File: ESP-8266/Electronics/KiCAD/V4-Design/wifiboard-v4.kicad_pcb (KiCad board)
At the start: 2 copper layers, 59 x 47 mm, 37 parts, among them IC1 78033AF, J1 PWR, J10 Conn_01x01_Male, J2 thermistor, J3 Aux1, J4 Aux2, J5 USB-3V3, J6 PROG, J7 OUT, J8 mains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

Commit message: SB & AB PCB layout
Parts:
- removed IC1: 78033AF, Package_TO_SOT_SMD:TO-252-2
- removed J10: Conn_01x01_Male, Connector_PinHeader_2.54mm:PinHeader_1x01_P2.54mm_Vertical
- added U2: 78033, Package_TO_SOT_SMD:TO-252-2, F.Cu at (50.9, 173.4)
- J9: value Conn_01x01_Male -> led-select; footprint Connector_PinHeader_2.54mm:PinHeader_1x01_P2.54mm_Vertical -> Connector_PinHeader_2.54mm:PinHeader_1x02_P2.54mm_Vertical
- moved R2 14.7 mm to (73.9, 158.6)
- moved R3 5.80 mm to (71.1, 144.3), turned to 270 degrees
- moved J9 2.67 mm to (48.0, 161.7), turned to 180 degrees
- moved C4 1.69 mm to (70.6, 140.0), turned to 90 degrees
- moved C1 1.63 mm to (39.2, 170.9)
- moved J1 1.27 mm to (30.1, 173.7)
- moved C3 1.19 mm to (63.0, 170.8)
- moved U1 0.09 mm to (67.1, 155.1)
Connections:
- R10 pad 1: Net-(J10-Pad1) -> Net-(J9-Pad1)
- R9 pad 2: Net-(J9-Pad1) -> Net-(J9-Pad2)
- U1 pad 14: Net-(J9-Pad1) -> Net-(J9-Pad2)
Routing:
- net +3V3: track 0.00 -> 129.2 mm, vias 0 -> 1
- net +12V: track 0.00 -> 68.6 mm
- net Net-(J5-Pad5): track 0.00 -> 38.6 mm
- net GND: track 0.00 -> 33.5 mm, vias 0 -> 2
- net Net-(J5-Pad4): track 0.00 -> 27.5 mm
- net Net-(J7-Pad2): track 0.00 -> 27.2 mm
- net Net-(C5-Pad1): track 0.00 -> 25.4 mm
- net Net-(C1-Pad1): track 0.00 -> 21.3 mm
- net Net-(J9-Pad2): track 0.00 -> 20.5 mm, vias 0 -> 1
- net Net-(C2-Pad1): track 0.00 -> 18.2 mm
- net Net-(J8-Pad2): track 0.00 -> 16.3 mm
- net Net-(J8-Pad1): track 0.00 -> 16.3 mm
- net Net-(J6-Pad2): track 0.00 -> 16.0 mm, vias 0 -> 2
- net Net-(R5-Pad2): track 0.00 -> 10.5 mm
- net Net-(J3-Pad1): track 0.00 -> 10.2 mm
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- added copper zone on B.Cu, net GND
- added copper zone on F.Cu, net GND
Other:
- board text added: "+12"
- board text added: "BLK"
- board text added: "GND"
- board text added: "GRN"
- board text added: "LED"
- board text added: "MAINS"
- board text added: "OUT"
- board text added: "PROG"
- board text added: "RESET"
- board text added: "Therm"
- board text added: "USB 3V3"

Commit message: PCB sent for trial production.
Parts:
- added JP1: SolderJumper_2_Bridged, Jumper:SolderJumper-2_P1.3mm_Bridged_RoundedPad1.0x1.5mm, F.Cu at (44.6, 160.4)
- moved R10 5.28 mm to (40.0, 163.4)
- moved J1 3.29 mm to (31.6, 176.7), turned to 270 degrees
- moved Q1 2.11 mm to (39.4, 144.4)
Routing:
- net Net-(J9-Pad2): track 20.5 -> 26.7 mm
- net Net-(J5-Pad5): track 38.6 -> 32.7 mm
- net Net-(J9-Pad1): track 3.76 -> 8.45 mm
- net Net-(J6-Pad2): track 16.0 -> 12.7 mm
- net Net-(Q1-Pad1): track 9.78 -> 12.1 mm
- net +3V3: track 129.2 -> 131.3 mm
- net Net-(J7-Pad2): track 27.2 -> 25.1 mm
- net Net-(D2-Pad2): track 2.52 -> 4.28 mm
- net +12V: track 68.6 -> 70.0 mm
- net Net-(C2-Pad1): track 18.2 -> 18.9 mm
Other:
- board text added: "L1"
- board text added: "L2"
- board text added: "POWER"

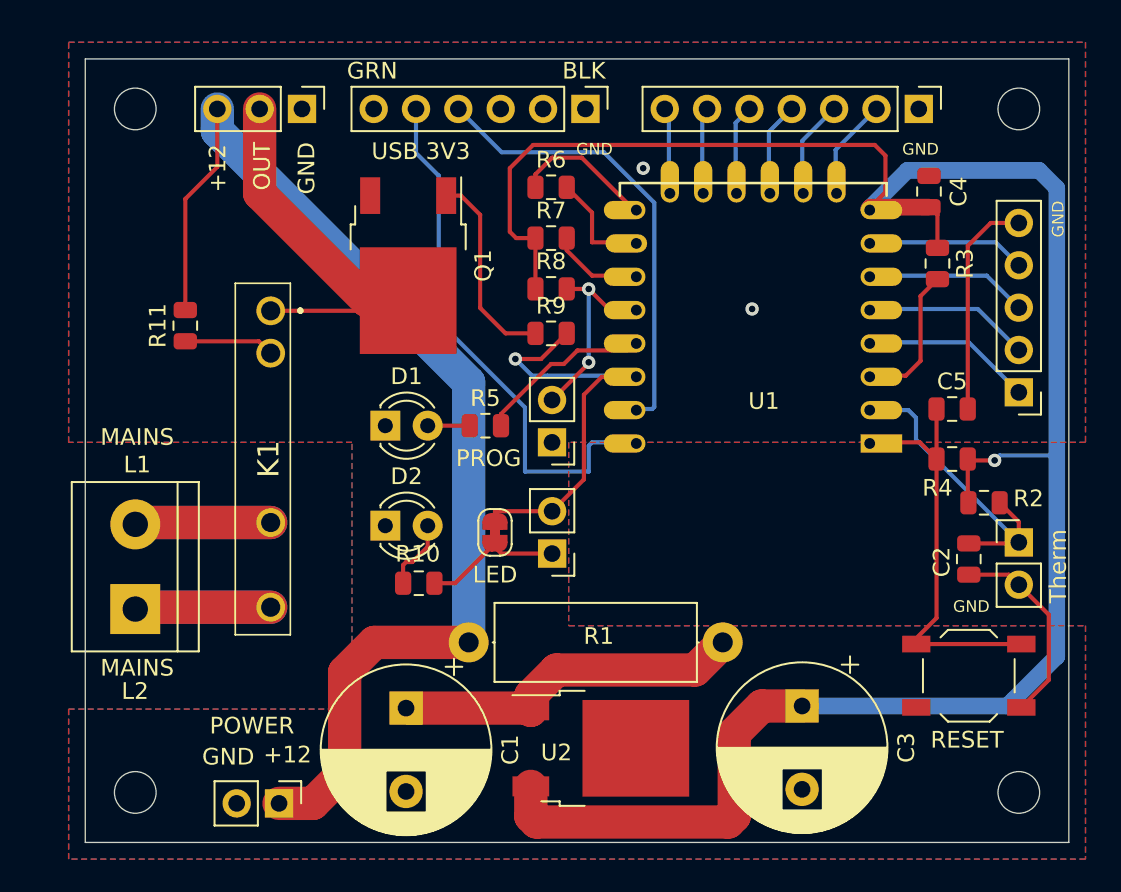
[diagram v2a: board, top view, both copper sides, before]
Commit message: PCB modified to accommodate relay as well as opto-SCR. GERBERS need to be updated.
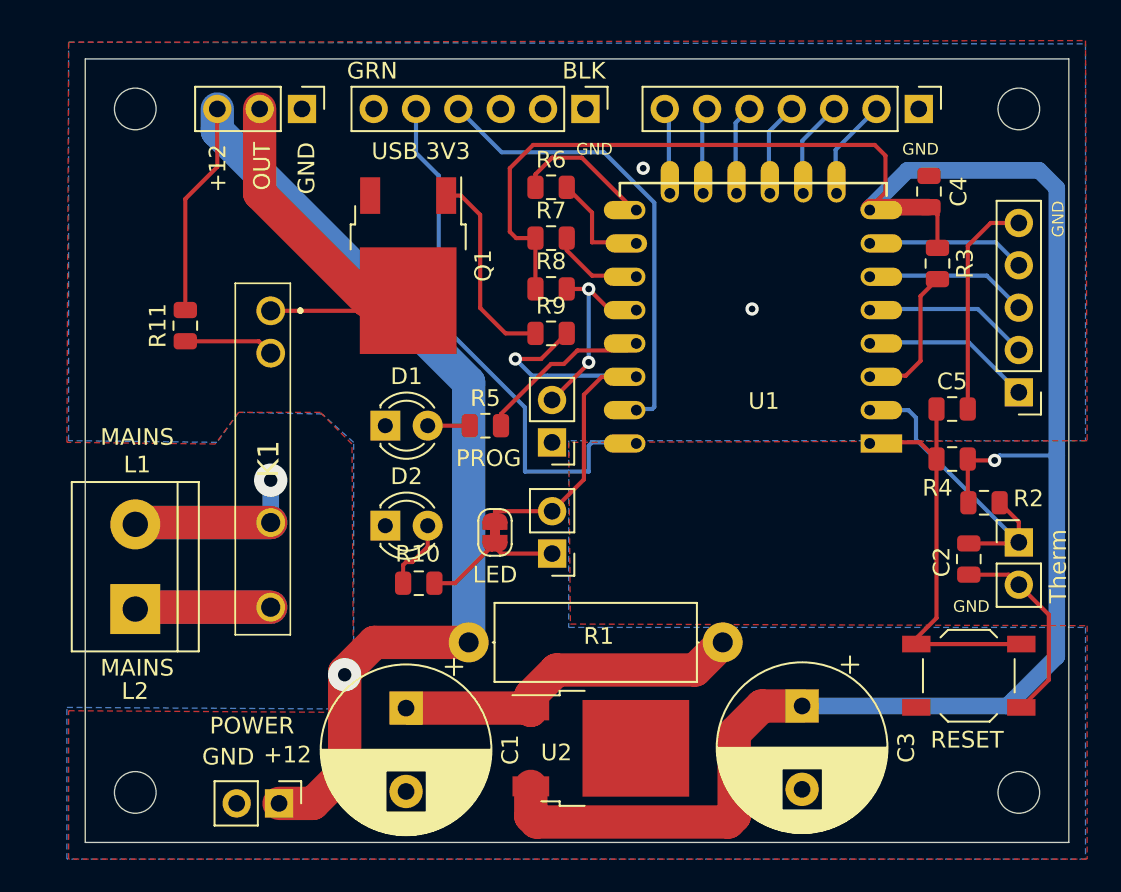
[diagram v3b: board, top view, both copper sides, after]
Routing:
- net Net-(J8-Pad2): track 16.3 -> 18.9 mm, vias 0 -> 1
- net +12V: vias 0 -> 1
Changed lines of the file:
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@@
-(kicad_pcb (version 20171130) (host pcbnew 5.1.6-c6e7f7d~87~ubuntu18.04.1)
+(kicad_pcb (version 20171130) (host pcbnew 5.1.5+dfsg1-2build2)
   (general
     (thickness 1.6)
-    (drawings 38)
-    (tracks 190)
+    (drawings 41)
+    (tracks 194)
     (zones 0)
     (modules 37)
@@
     (47 F.CrtYd user)
     (48 B.Fab user)
-    (49 F.Fab user hide)
+    (49 F.Fab user)
   )
   (setup
-    (last_trace_width 0.25)
+    (last_trace_width 1)
     (user_trace_width 1)
     (user_trace_width 2)
@@
     (via_min_size 0.4)
     (via_min_drill 0.3)
+    (user_via 2 0.8)
     (uvia_size 0.3)
     (uvia_drill 0.1)
@@
       ))
   )
+  (gr_line (start 27.8 155) (end 19 155) (layer Eco2.User) (width 0.15))
+  (gr_line (start 34 153.2) (end 36 155) (layer Eco2.User) (width 0.15))
+  (gr_line (start 29.2 153.2) (end 34 153.2) (layer Eco2.User) (width 0.15))
+  (gr_line (start 27.8 155) (end 29.2 153.2) (layer Eco2.User) (width 0.15))
   (gr_text POWER (at 30 172) (layer F.SilkS)
     (effects (font (size 1 1) (thickness 0.15)))
@@
   (gr_line (start 49 155) (end 49 166) (layer Eco2.User) (width 0.15))
   (gr_line (start 19 155) (end 19 131) (layer Eco2.User) (width 0.15))
-  (gr_line (start 36 155) (end 19 155) (layer Eco2.User) (width 0.15))
   (gr_line (start 36 171) (end 36 155) (layer Eco2.User) (width 0.15))
   (gr_line (start 19 171) (end 36 171) (layer Eco2.User) (width 0.15))
@@
   (gr_line (start 79 132) (end 79 179) (layer Edge.Cuts) (width 0.05))
   (gr_line (start 20 132) (end 79 132) (layer Edge.Cuts) (width 0.05))
+  (via (at 31.123 157.27) (size 2) (drill 0.8) (layers F.Cu B.Cu) (net 26))
   (segment (start 75.3975 162.9375) (end 76 163.54) (width 0.25) (layer F.Cu) (net 1))
   (segment (start 73 162.9375) (end 75.3975 162.9375) (width 0.25) (layer F.Cu) (net 1))
@@
   (segment (start 37.343 167) (end 43 167) (width 2) (layer F.Cu) (net 8))
   (segment (start 35.56 168.783) (end 37.343 167) (width 2) (layer F.Cu) (net 8))
-  (segment (start 35.56 174.752) (end 35.56 168.783) (width 2) (layer F.Cu) (net 8))
+  (segment (start 35.56 174.752) (end 35.56 168.94) (width 2) (layer F.Cu) (net 8))
   (segment (start 33.655 176.657) (end 35.56 174.752) (width 2) (layer F.Cu) (net 8))
   (segment (start 31.623 176.657) (end 33.655 176.657) (width 2) (layer F.Cu) (net 8))
+  (segment (start 35.56 168.94) (end 35.56 168.783) (width 2) (layer F.Cu) (net 8))
+  (via (at 35.56 168.94) (size 2) (drill 0.8) (layers F.Cu B.Cu) (net 8))
   (segment (start 73 149) (end 76 152) (width 0.25) (layer B.Cu) (net 9))
   (segment (start 67 149) (end 73 149) (width 0.25) (layer B.Cu) (net 9))
@@
   (segment (start 23.07 159.81) (end 22.987 159.893) (width 2) (layer F.Cu) (net 26))
   (segment (start 31.123 159.81) (end 23.07 159.81) (width 2) (layer F.Cu) (net 26))
+  (segment (start 31.123 159.81) (end 31.123 157.27) (width 1) (layer B.Cu) (net 26))
   (segment (start 30.4105 148.9375) (end 31.123 149.65) (width 0.25) (layer F.Cu) (net 27))
   (segment (start 26 148.9375) (end 30.4105 148.9375) (width 0.25) (layer F.Cu) (net 27))
@@
     (polygon
       (pts
-        (xy 80 155) (xy 49 155) (xy 49 166) (xy 80 166) (xy 80 180)
-        (xy 19 180) (xy 19 171) (xy 36 171) (xy 36 155) (xy 19 155)
-        (xy 19 131) (xy 80 131)
+        (xy 80.1 154.9) (xy 49 155) (xy 49.1 165.9) (xy 80.1 166) (xy 80.1 180)
+        (xy 19 180) (xy 19 171.1) (xy 36.1 171.2) (xy 36 155.1) (xy 34.1 153.2)
+        (xy 29.2 153.2) (xy 27.8 155.1) (xy 18.9 155) (xy 19 131) (xy 80 130.9)
       )
     )
@@
     (polygon
       (pts
-        (xy 80 155) (xy 49 155) (xy 49 166) (xy 80 166) (xy 80 180)
-        (xy 19 180) (xy 19 171) (xy 36 171) (xy 36 155) (xy 19 155)
-        (xy 19 131) (xy 80 131)
+        (xy 80 131.1) (xy 80 154.9) (xy 49 154.9) (xy 49 166.1) (xy 80 166.1)
+        (xy 80 180) (xy 18.9 180) (xy 18.9 170.9) (xy 36.1 171) (xy 36.1 155)
+        (xy 34.2 153.3) (xy 29.2 153.2) (xy 27.9 155) (xy 19 154.9) (xy 19 131)
       )
     )
